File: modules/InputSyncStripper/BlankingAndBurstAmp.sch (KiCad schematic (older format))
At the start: 55 parts

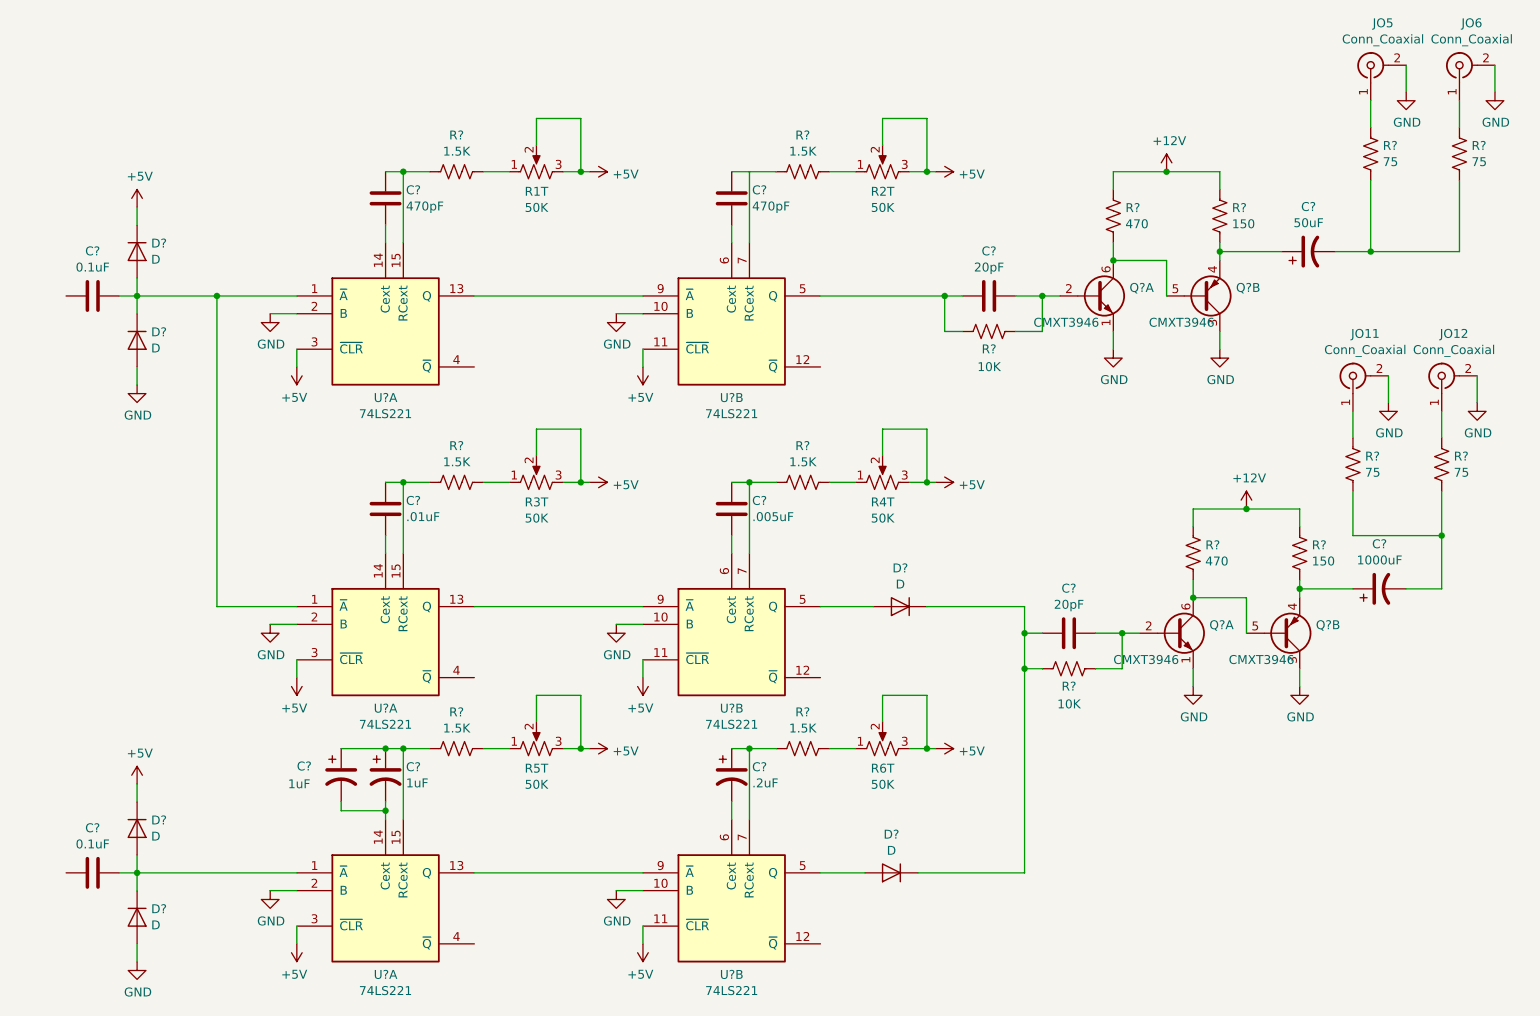
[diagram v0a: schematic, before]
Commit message: fix some ERC issues; assign symbols
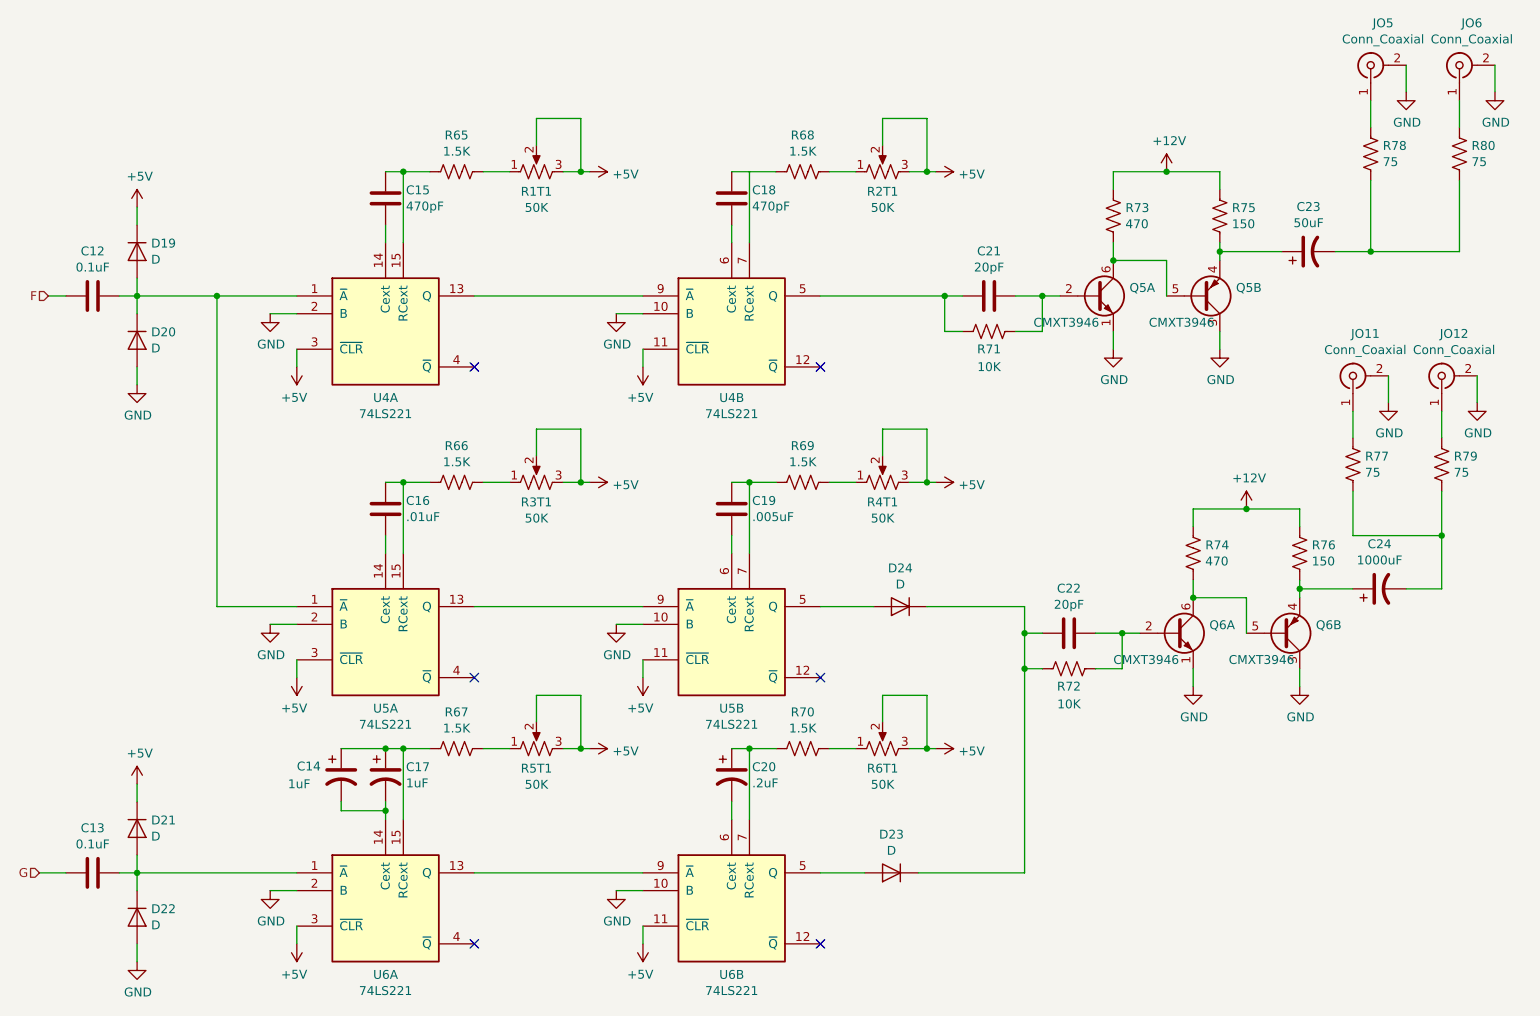
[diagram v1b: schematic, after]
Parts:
- gave numbers to parts that had none: 40
- renumbered R1T to R1T1, R2T to R2T1, R3T to R3T1, R4T to R4T1, R5T to R5T1, R6T to R6T1
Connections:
- net F: now reaches C12.2
- net G: now reaches C13.2
- no-connect marks 0 -> 6

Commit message: Find and fix missing values
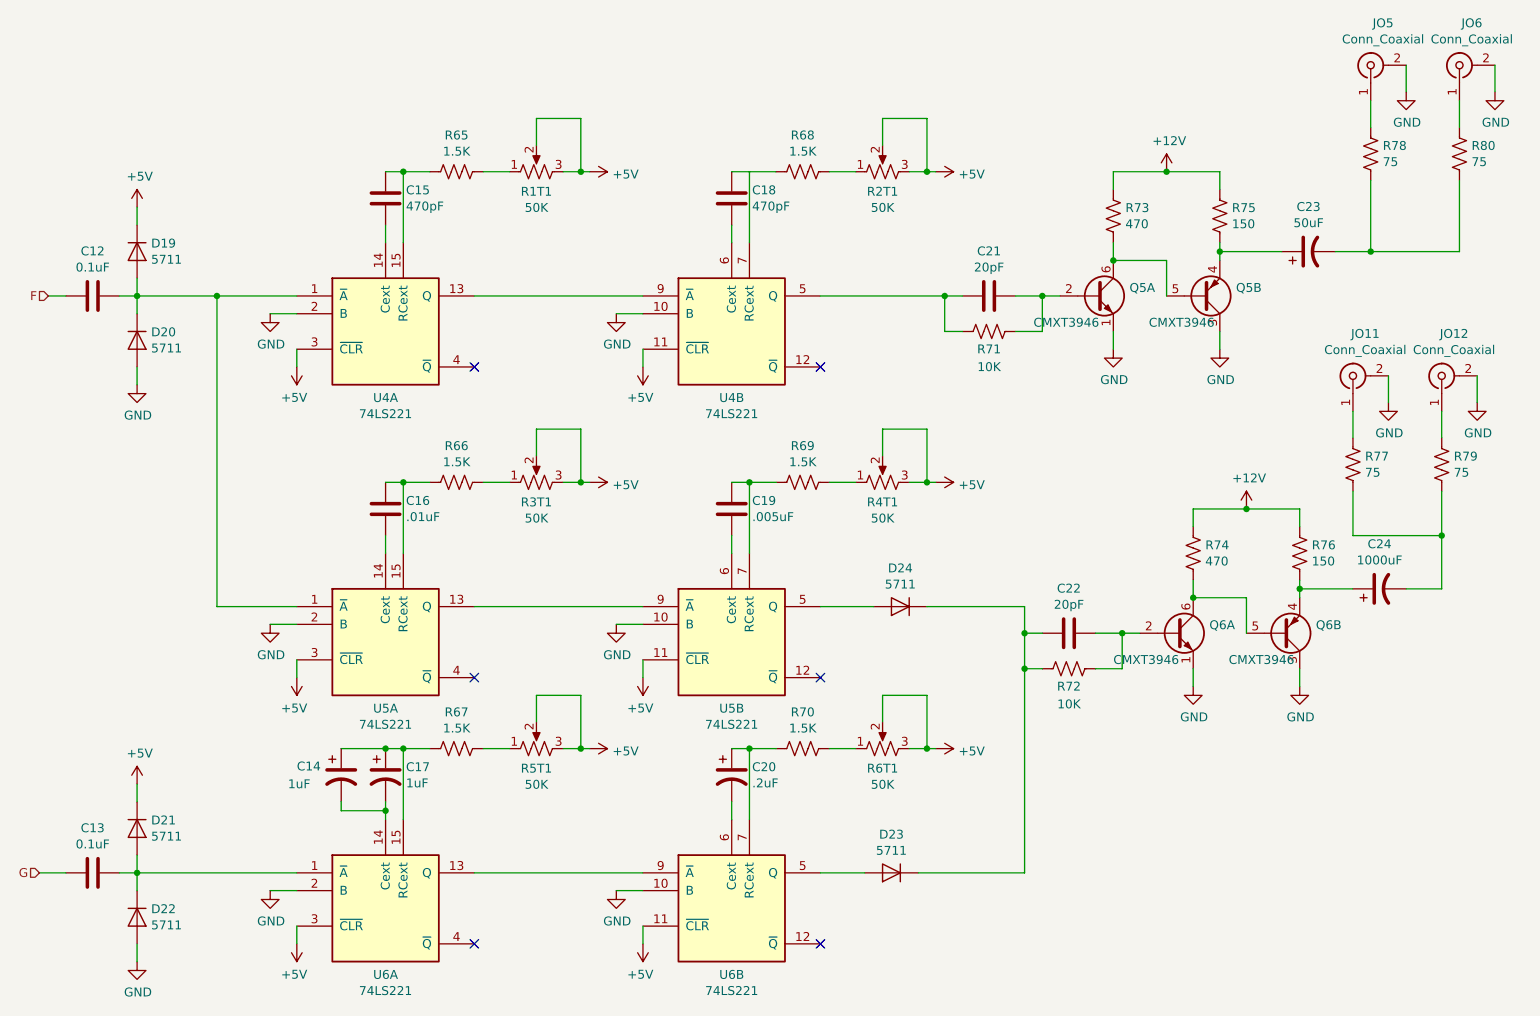
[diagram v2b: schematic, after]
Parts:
- D19, D20, D21, D22, D23, D24: value D -> 5711
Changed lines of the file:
@@
 P 2600 2250
 F 0 "D19" V 2554 2329 50  0000 L CNN
-F 1 "D" V 2645 2329 50  0000 L CNN
+F 1 "5711" V 2645 2329 50  0000 L CNN
 F 2 "" H 2600 2250 50  0001 C CNN
 F 3 "~" H 2600 2250 50  0001 C CNN
@@
 P 2600 2750
 F 0 "D20" V 2554 2829 50  0000 L CNN
-F 1 "D" V 2645 2829 50  0000 L CNN
+F 1 "5711" V 2645 2829 50  0000 L CNN
 F 2 "" H 2600 2750 50  0001 C CNN
 F 3 "~" H 2600 2750 50  0001 C CNN
@@
 P 2600 5500
 F 0 "D21" V 2554 5579 50  0000 L CNN
-F 1 "D" V 2645 5579 50  0000 L CNN
+F 1 "5711" V 2645 5579 50  0000 L CNN
 F 2 "" H 2600 5500 50  0001 C CNN
 F 3 "~" H 2600 5500 50  0001 C CNN
@@
 P 2600 6000
 F 0 "D22" V 2554 6079 50  0000 L CNN
-F 1 "D" V 2645 6079 50  0000 L CNN
+F 1 "5711" V 2645 6079 50  0000 L CNN
 F 2 "" H 2600 6000 50  0001 C CNN
 F 3 "~" H 2600 6000 50  0001 C CNN
@@
 P 6900 4250
 F 0 "D24" H 6900 4034 50  0000 C CNN
-F 1 "D" H 6900 4125 50  0000 C CNN
+F 1 "5711" H 6900 4125 50  0000 C CNN
 F 2 "" H 6900 4250 50  0001 C CNN
 F 3 "~" H 6900 4250 50  0001 C CNN
@@
 P 6850 5750
 F 0 "D23" H 6850 5534 50  0000 C CNN
-F 1 "D" H 6850 5625 50  0000 C CNN
+F 1 "5711" H 6850 5625 50  0000 C CNN
 F 2 "" H 6850 5750 50  0001 C CNN
 F 3 "~" H 6850 5750 50  0001 C CNN

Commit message: building out footprints/BOM
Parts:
- C12, C13, C15, C16, C18, C21, C22: footprint (none) -> Capacitor_SMD:C_0805_2012Metric_Pad1.15x1.40mm_HandSolder
- C14, C17: footprint (none) -> Capacitor_SMD:CP_Elec_4x5.4
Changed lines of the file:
@@
 F 0 "C12" V 2098 2500 50  0000 C CNN
 F 1 "0.1uF" V 2189 2500 50  0000 C CNN
-F 2 "" H 2388 2350 50  0001 C CNN
+F 2 "Capacitor_SMD:C_0805_2012Metric_Pad1.15x1.40mm_HandSolder" H 2388 2350 50  0001 C CNN
 F 3 "~" H 2350 2500 50  0001 C CNN
 	1    2350 2500
@@
 F 0 "C13" V 2098 5750 50  0000 C CNN
 F 1 "0.1uF" V 2189 5750 50  0000 C CNN
-F 2 "" H 2388 5600 50  0001 C CNN
+F 2 "Capacitor_SMD:C_0805_2012Metric_Pad1.15x1.40mm_HandSolder" H 2388 5600 50  0001 C CNN
 F 3 "~" H 2350 5750 50  0001 C CNN
 	1    2350 5750
@@
 F 0 "C15" H 4115 1996 50  0000 L CNN
 F 1 "470pF" H 4115 1905 50  0000 L CNN
-F 2 "" H 4038 1800 50  0001 C CNN
+F 2 "Capacitor_SMD:C_0805_2012Metric_Pad1.15x1.40mm_HandSolder" H 4038 1800 50  0001 C CNN
 F 3 "~" H 4000 1950 50  0001 C CNN
 	1    4000 1950
@@
 F 0 "C18" H 6065 1996 50  0000 L CNN
 F 1 "470pF" H 6065 1905 50  0000 L CNN
-F 2 "" H 5988 1800 50  0001 C CNN
+F 2 "Capacitor_SMD:C_0805_2012Metric_Pad1.15x1.40mm_HandSolder" H 5988 1800 50  0001 C CNN
 F 3 "~" H 5950 1950 50  0001 C CNN
 	1    5950 1950
@@
 F 0 "C16" H 4115 3746 50  0000 L CNN
 F 1 ".01uF" H 4115 3655 50  0000 L CNN
-F 2 "" H 4038 3550 50  0001 C CNN
+F 2 "Capacitor_SMD:C_0805_2012Metric_Pad1.15x1.40mm_HandSolder" H 4038 3550 50  0001 C CNN
 F 3 "~" H 4000 3700 50  0001 C CNN
 	1    4000 3700
@@
 F 0 "C17" H 4115 5246 50  0000 L CNN
 F 1 "1uF" H 4115 5155 50  0000 L CNN
-F 2 "" H 4000 5200 50  0001 C CNN
+F 2 "Capacitor_SMD:CP_Elec_4x5.4" H 4000 5200 50  0001 C CNN
 F 3 "~" H 4000 5200 50  0001 C CNN
 	1    4000 5200
@@
 F 0 "C14" H 3500 5250 50  0000 L CNN
 F 1 "1uF" H 3450 5150 50  0000 L CNN
-F 2 "" H 3750 5200 50  0001 C CNN
+F 2 "Capacitor_SMD:CP_Elec_4x5.4" H 3750 5200 50  0001 C CNN
 F 3 "~" H 3750 5200 50  0001 C CNN
 	1    3750 5200
@@
 F 0 "C22" V 7598 4400 50  0000 C CNN
 F 1 "20pF" V 7689 4400 50  0000 C CNN
-F 2 "" H 7888 4250 50  0001 C CNN
+F 2 "Capacitor_SMD:C_0805_2012Metric_Pad1.15x1.40mm_HandSolder" H 7888 4250 50  0001 C CNN
 F 3 "~" H 7850 4400 50  0001 C CNN
 	1    7850 4400
@@
 F 0 "C21" V 7148 2500 50  0000 C CNN
 F 1 "20pF" V 7239 2500 50  0000 C CNN
-F 2 "" H 7438 2350 50  0001 C CNN
+F 2 "Capacitor_SMD:C_0805_2012Metric_Pad1.15x1.40mm_HandSolder" H 7438 2350 50  0001 C CNN
 F 3 "~" H 7400 2500 50  0001 C CNN
 	1    7400 2500
